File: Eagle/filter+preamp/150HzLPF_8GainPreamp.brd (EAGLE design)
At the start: 66 x 42 mm, 25 parts, among them U1 LM358, U2 LM358

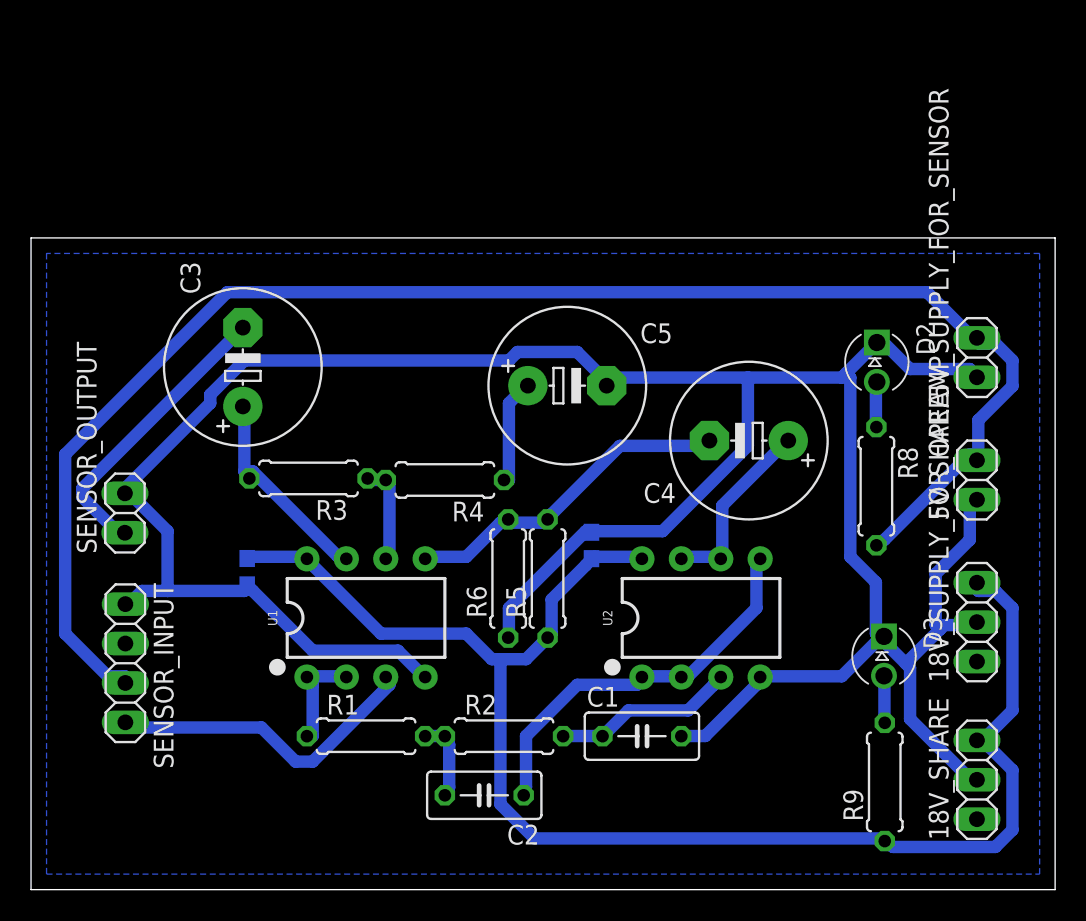
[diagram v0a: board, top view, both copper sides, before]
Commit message: add passcon
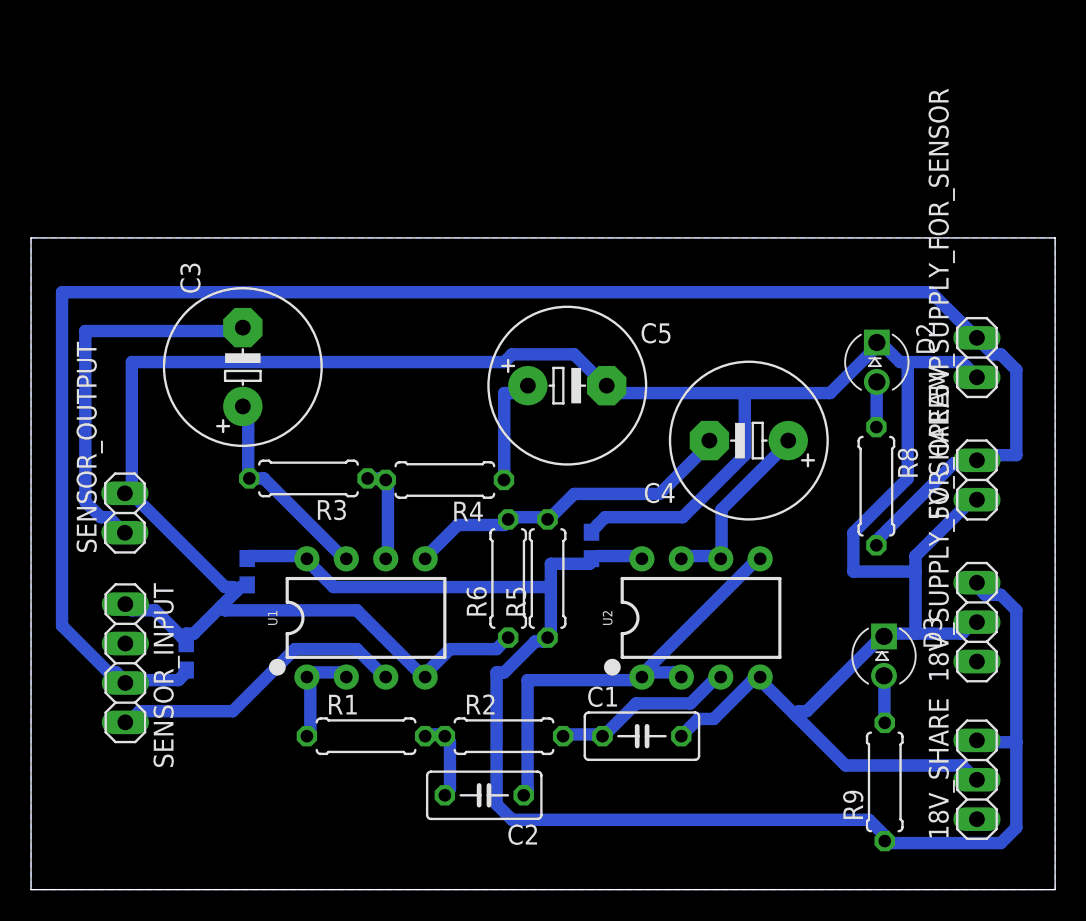
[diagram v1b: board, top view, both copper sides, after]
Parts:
- added C6: 0.1u, rcl:C0603
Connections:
- net N$6 renamed 18V_VCC
- removed net N$15: 5V_SHARE.2, 5V_SUPPLY_FOR_SENSOR.2, R8.2, SENSOR_INPUT.3
- removed net N$17: 18V_SHARE.2, 18V_SUPPLY_FOR_OPEAMP.2, 5V_SHARE.1, 5V_SUPPLY_FOR_SENSOR.1, C1.2, C5.-, C8.2, C9.2, D2.C, D3.C, R6.1, SENSOR_INPUT.1, SENSOR_OUTPUT.2, U1.4, U2.4
- new net 5V_VCC: 5V_SHARE.2, 5V_SUPPLY_FOR_SENSOR.2, C6.1, R8.2, SENSOR_INPUT.3
- new net GND: 18V_SHARE.2, 18V_SUPPLY_FOR_OPEAMP.2, 5V_SHARE.1, 5V_SUPPLY_FOR_SENSOR.1, C1.2, C5.-, C6.2, C8.2, C9.2, D2.C, D3.C, R6.1, SENSOR_INPUT.1, SENSOR_OUTPUT.2, U1.4, U2.4
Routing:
- net GND: track 0.00 -> 191.6 mm
- net N$17: track 179.6 -> 0.00 mm
- net 5V_VCC: track 0.00 -> 112.2 mm
- net N$15: track 100.6 -> 0.00 mm
- net N$13: track 19.0 -> 24.6 mm
- net 18V_VCC: track 96.3 -> 99.4 mm
- net N$4: track 25.4 -> 28.2 mm
- net N$5: track 20.6 -> 19.4 mm
- net N$11: track 6.95 -> 7.58 mm
